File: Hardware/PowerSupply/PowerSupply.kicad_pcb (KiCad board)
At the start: 2 copper layers, 83 x 95 mm, 31 parts, among them SW31 SW_DPDT_x2

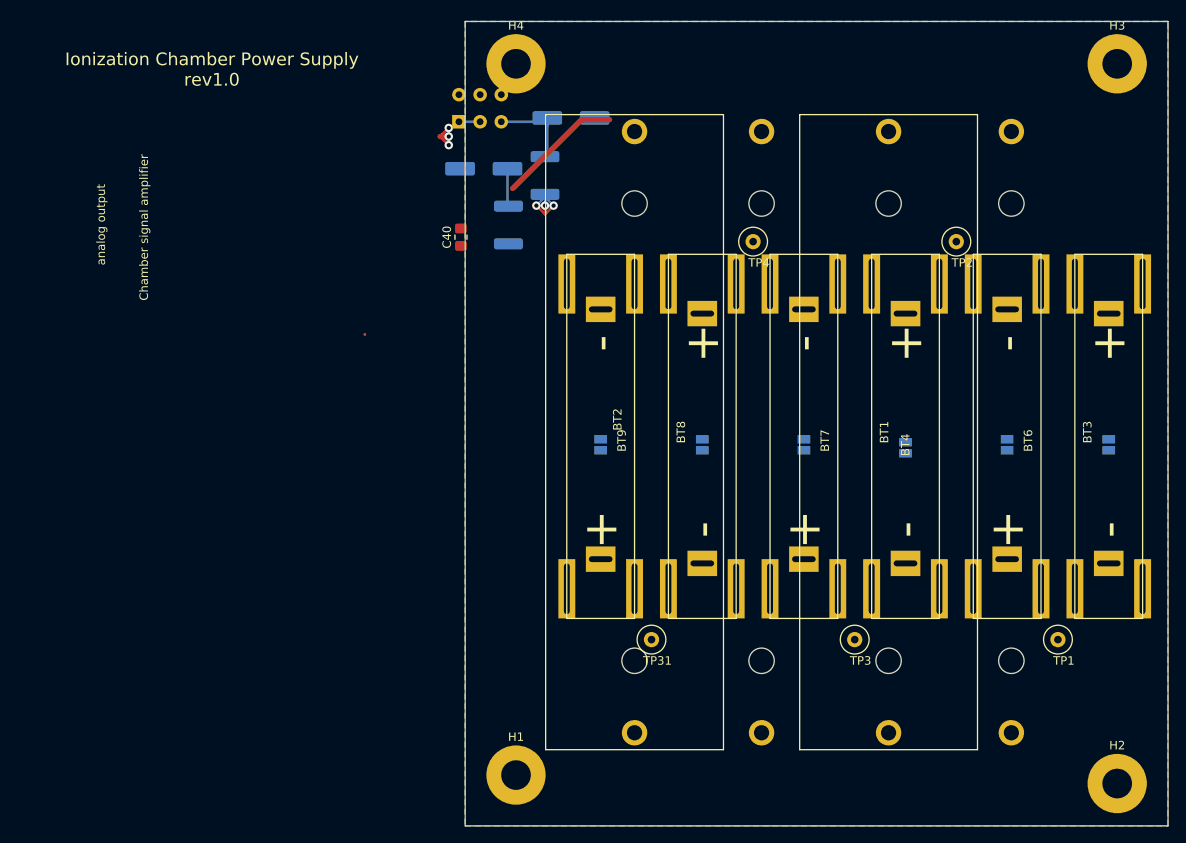
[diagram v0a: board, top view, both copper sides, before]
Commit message: finished design of the power power supply pcb
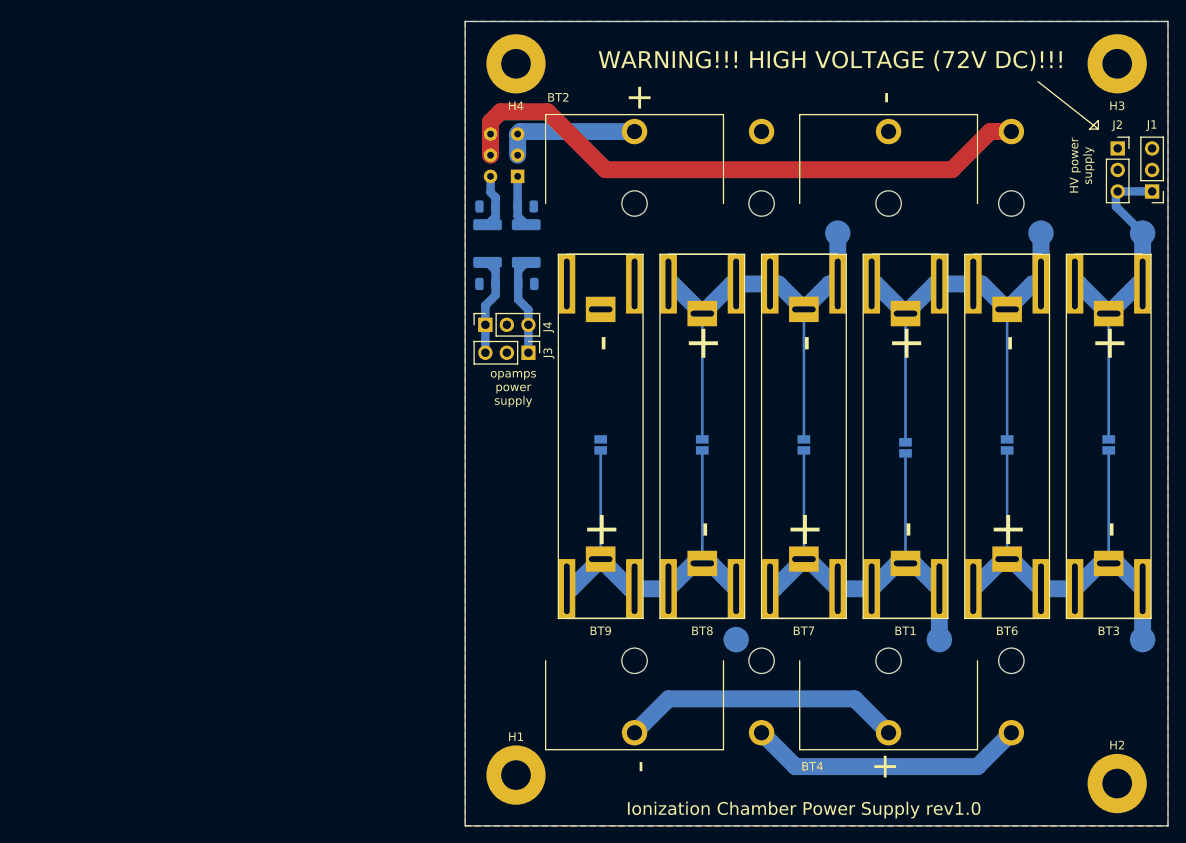
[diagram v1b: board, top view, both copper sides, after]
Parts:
- removed C33, C34: 100u/16V, Capacitor_SMD:CP_Elec_6.3x5.4
- added C1: 100n, Capacitor_SMD:C_0805_2012Metric, B.Cu at (135.6, 95.0)
- added C2: 100n, Capacitor_SMD:C_0805_2012Metric, B.Cu at (140.1, 85.9)
- added C3: 100n, Capacitor_SMD:C_0805_2012Metric, B.Cu at (135.6, 85.9)
- added J1: Conn_01x03_Male, Connector_PinHeader_2.54mm:PinHeader_1x03_P2.54mm_Vertical, F.Cu at (214.1, 84.1)
- added J2: Conn_01x03_Female, Connector_PinSocket_2.54mm:PinSocket_1x03_P2.54mm_Vertical, F.Cu at (210.1, 79.0)
- added J3: Conn_01x03_Male, Connector_PinHeader_2.54mm:PinHeader_1x03_P2.54mm_Vertical, F.Cu at (140.5, 103.1)
- added J4: Conn_01x03_Female, Connector_PinSocket_2.54mm:PinSocket_1x03_P2.54mm_Vertical, F.Cu at (135.4, 99.8)
- added TP5: TestPoint, TestPoint:TestPoint_Pad_D3.0mm, B.Cu at (213.0, 89.0)
- C40: footprint Capacitor_SMD:C_0805_2012Metric_Pad1.15x1.40mm_HandSolder -> Capacitor_SMD:C_0805_2012Metric; moved to B.Cu
- TP1, TP2, TP3, TP31, TP4: footprint TestPoint:TestPoint_Loop_D2.60mm_Drill0.9mm_Beaded -> TestPoint:TestPoint_Pad_D3.0mm; moved to B.Cu
- moved TP2 10.0 mm to (201.0, 89.0)
- moved TP4 10.0 mm to (177.0, 89.0)
- moved TP1 10.0 mm to (213.0, 137.0)
- moved TP3 10.0 mm to (189.0, 137.0)
- moved TP31 10.0 mm to (165.0, 137.0)
- moved C40 9.48 mm to (140.2, 95.0), turned to 180 degrees
- moved SW31 9.47 mm to (139.2, 82.3), turned to 90 degrees
- moved L32 8.34 mm to (140.2, 90.2)
- moved L33 3.30 mm to (135.6, 90.2)
- turned JP2 to 90 degrees
- turned JP4 to 90 degrees
- turned JP5 to 270 degrees
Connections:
- L32 pad 2: Net-(C33-Pad1) -> Net-(C2-Pad2)
- L33 pad 1: (no net) -> -BATT
- L33 pad 2: Net-(C34-Pad2) -> Net-(C3-Pad1)
- SW31 pad 1: Net-(BT2-Pad1) -> Net-(C2-Pad2)
- SW31 pad 3: Net-(C33-Pad1) -> Net-(BT2-Pad1)
- SW31 pad 4: Net-(BT32-Pad2) -> Net-(C3-Pad1)
- SW31 pad 6: Net-(C34-Pad2) -> Net-(BT32-Pad2)
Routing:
- net Net-(BT32-Pad2): track 0.00 -> 70.6 mm
- net Net-(BT1-Pad1): track 0.00 -> 61.9 mm
- net Net-(BT7-Pad2): track 0.00 -> 61.6 mm
- net Net-(BT3-Pad2): track 0.00 -> 57.6 mm
- net Net-(BT1-Pad2): track 0.00 -> 57.2 mm
- net Net-(BT8-Pad2): track 0.00 -> 51.6 mm
- net Net-(BT3-Pad1): track 0.00 -> 42.1 mm
- net Net-(BT2-Pad2): track 0.00 -> 33.3 mm
- net Net-(BT32-Pad1): track 0.00 -> 32.8 mm
- net GND: track 24.4 -> 0.00 mm, vias 3 -> 0
- net Net-(BT2-Pad1): track 2.50 -> 16.4 mm
- net -BATT: track 0.00 -> 11.6 mm
- net Net-(C33-Pad1): track 11.2 -> 0.00 mm
- net Net-(C3-Pad1): track 0.00 -> 6.35 mm
- net Net-(C2-Pad2): track 0.00 -> 6.13 mm
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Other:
- board text added: "Connect jumpes only if battery is not present in the socket."
- board text added: "HV power supply"
- board text added: "WARNING!!! HIGH VOLTAGE (72V DC)!!!"
- board text added: "opamps power supply"
- board text removed: "Chamber signal amplifier"
- board text removed: "analog output"

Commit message: draft of sensor pcb
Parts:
- moved J4 6.65 mm to (138.6, 105.6), turned to 180 degrees
- moved J3 2.81 mm to (141.7, 100.6), turned to 0 degrees
- moved H1 0.71 mm to (138.5, 153.5)
- moved H2 0.71 mm to (210.5, 153.5)
- moved H3 0.64 mm to (210.4, 69.5)
- moved H4 0.64 mm to (138.5, 69.4)
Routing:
- net -BATT: track 11.6 -> 19.2 mm
- net +BATT: track 11.6 -> 12.6 mm
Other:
- board text added: "Connect jumpers only if battery is not present in the socket."
- board text removed: "Connect jumpes only if battery is not present in the socket."

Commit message: fix #249, fix #251
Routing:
- net Net-(BT8-Pad2): track 51.6 -> 60.3 mm
- net Net-(BT7-Pad2): track 61.6 -> 65.3 mm
- net Net-(BT3-Pad1): track 42.1 -> 44.9 mm
- net Net-(BT1-Pad1): track 61.9 -> 64.6 mm
- net Net-(BT1-Pad2): track 57.2 -> 58.8 mm
- net Net-(BT3-Pad2): track 57.6 -> 58.8 mm
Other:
- board text added: "+"
- board text added: "-"
- board text added: "GND"
- board text added: "NC"
- board text added: "power supply for amplifier"
- board text removed: "opamps power supply"

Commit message: cleanup after transition to KiCad6
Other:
- net class Default removed
- net class high voltage removed
